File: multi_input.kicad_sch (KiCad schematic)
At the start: 6 parts

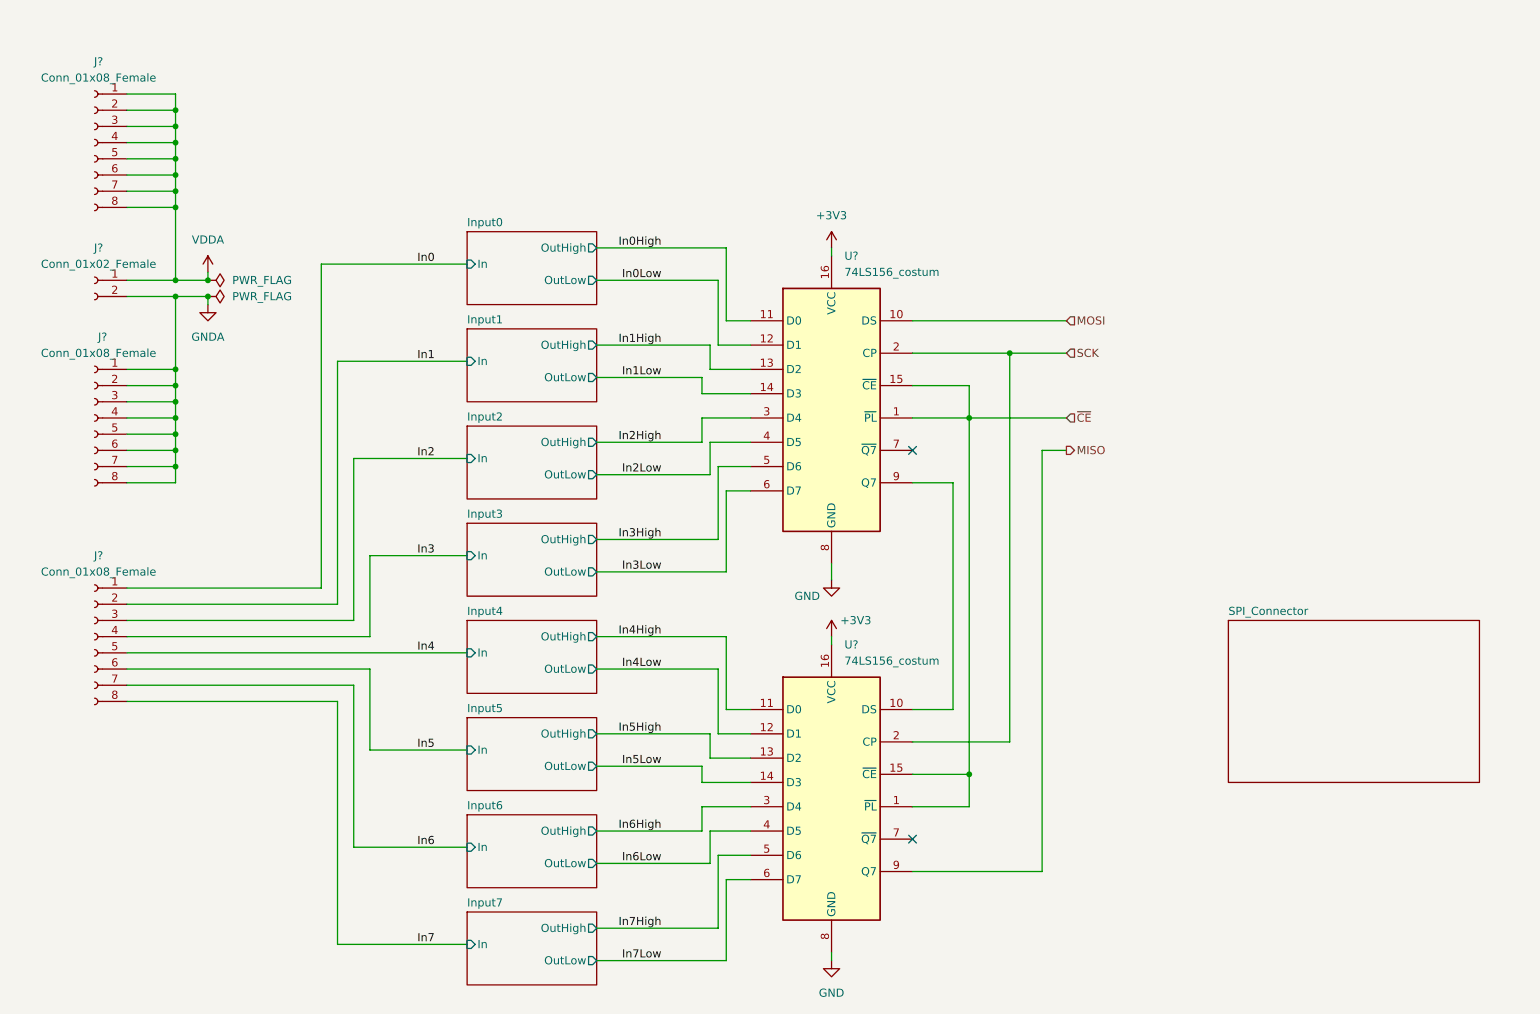
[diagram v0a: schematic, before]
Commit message: Schematic: Improve spi connector
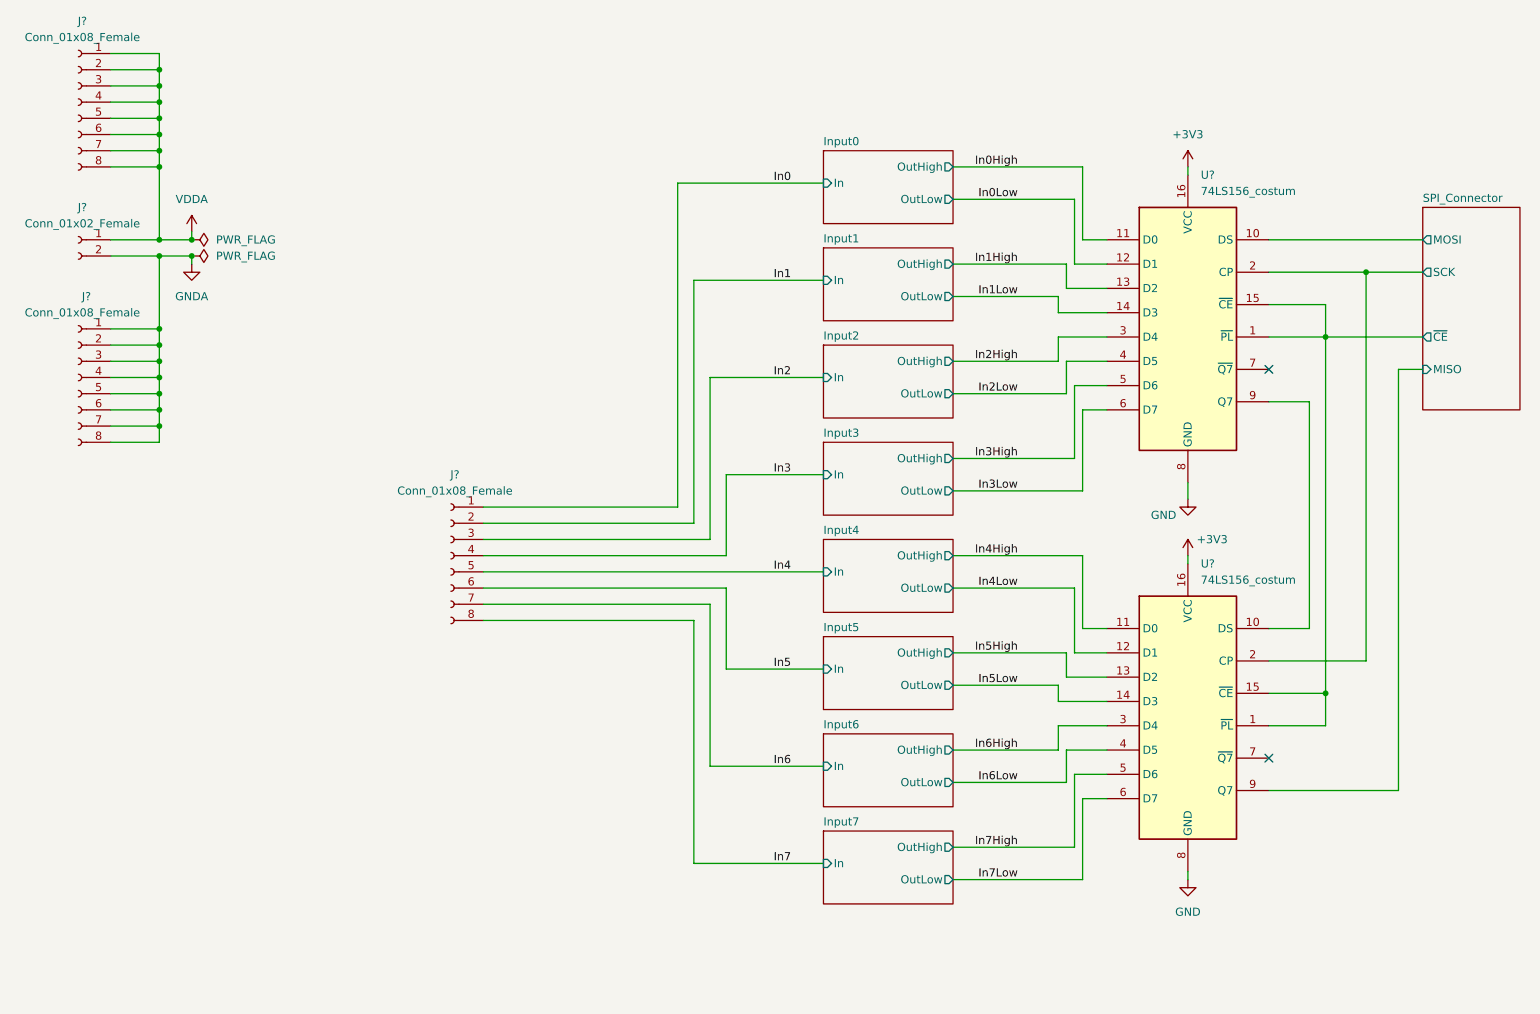
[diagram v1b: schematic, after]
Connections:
- net MISO renamed SPI_Connector/MISO
- net MOSI renamed SPI_Connector/MOSI
- net SCK renamed SPI_Connector/SCK
- net ~{CE} renamed SPI_Connector/~{CE}
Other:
- sheet SPI_Connector ports: added MISO, MOSI, SCK, ~{CE}; removed none
- moved on the sheet: J?, U?
